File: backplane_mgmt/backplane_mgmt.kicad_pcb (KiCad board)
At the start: 2 copper layers, 160 x 100 mm, 86 parts, among them J101 AudioJack3, J201 Backplane, J304 VIn, Q301 SUD19P06-60, Q302 SUD19P06-60, U101 LM833, U203 AT24CS32-SSHM, U301 AZ1117CD-5.0, U302 PTH08T220, U303 INA260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

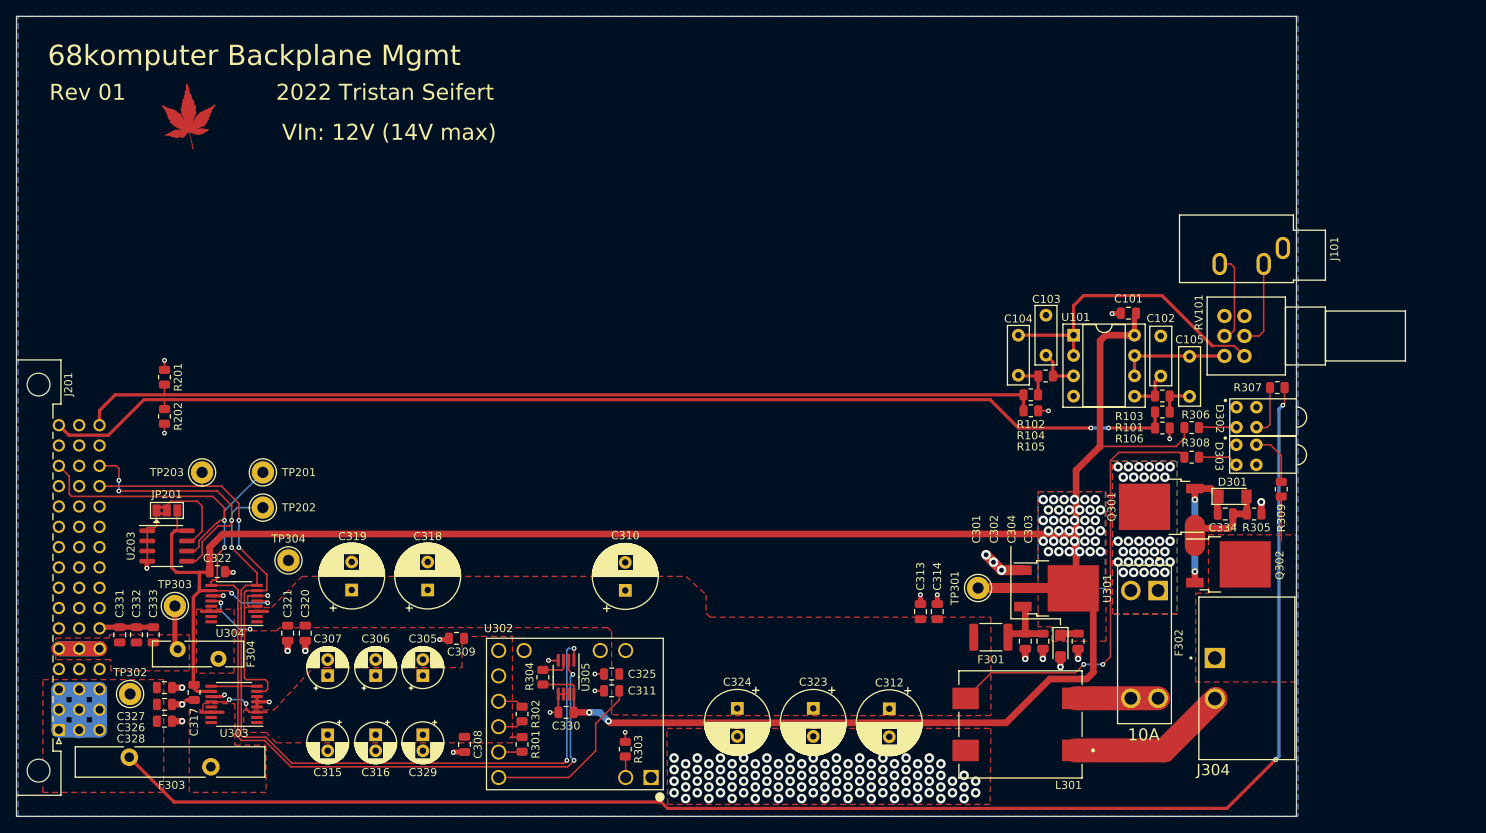
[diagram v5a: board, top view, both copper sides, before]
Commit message: Added +12V regulator to backplane mgmt
- Added the components for a discrete switching regulator (that is, with
  external switching MOSFETs, but a fancy little switching controller)
  to generate the 12V rail, at up to 10A. This is then further regulated
  to provide 5V for the board itself, and for the rest of the system.
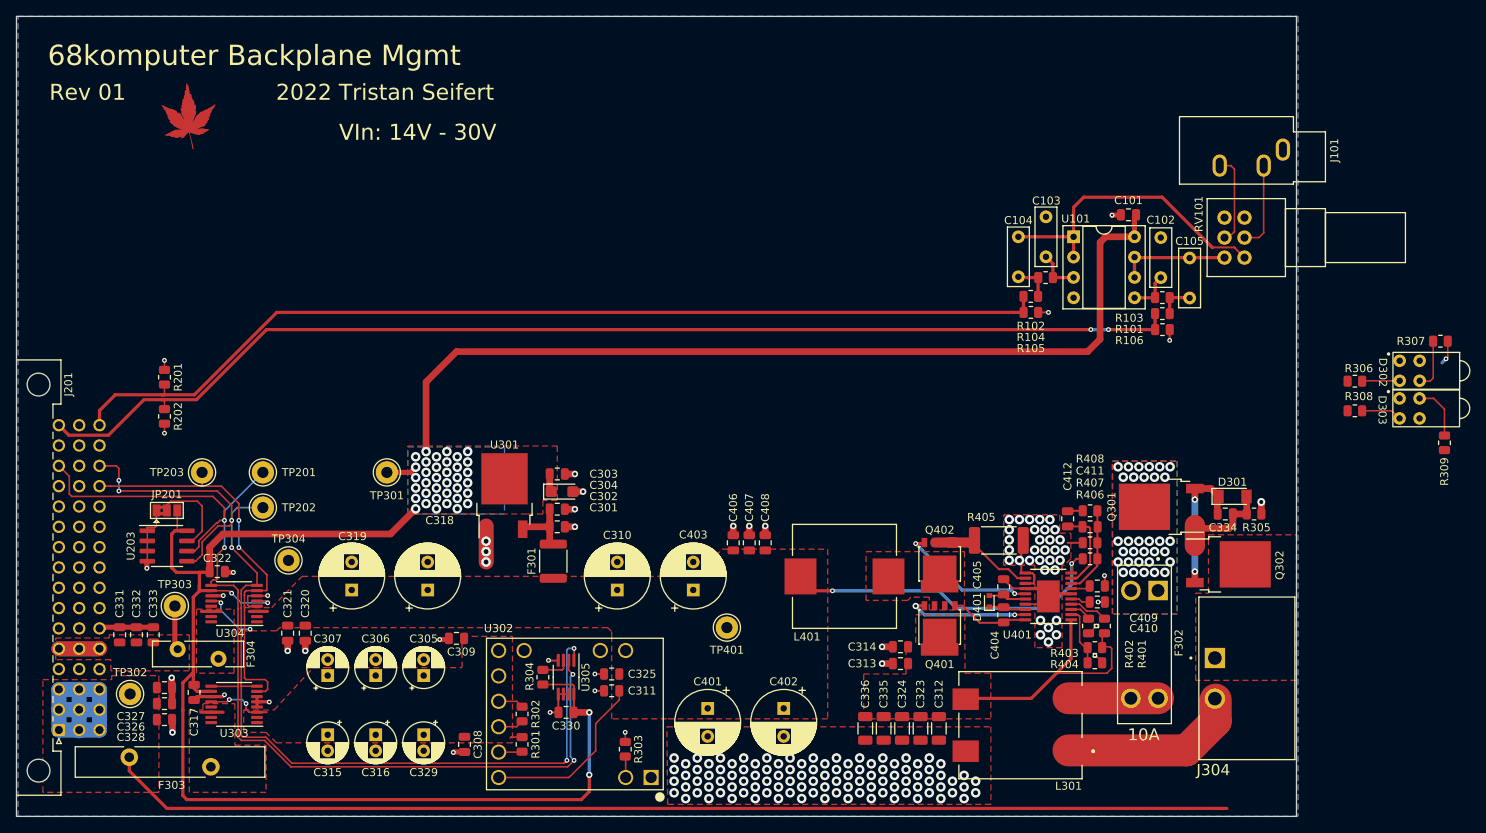
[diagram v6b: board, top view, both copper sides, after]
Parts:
- added C335: 2.2µF, Capacitor_SMD:C_1206_3216Metric, F.Cu at (138.4, 109.0)
- added C336: 2.2µF, Capacitor_SMD:C_1206_3216Metric, F.Cu at (136.1, 109.0)
- added C401: 330µF, Capacitor_THT:CP_Radial_D8.0mm_P3.50mm, F.Cu at (116.4, 106.5)
- added C402: 330µF, Capacitor_THT:CP_Radial_D8.0mm_P3.50mm, F.Cu at (125.9, 106.5)
- added C403: 330µF, Capacitor_THT:CP_Radial_D8.0mm_P3.50mm, F.Cu at (114.6, 91.7)
- added C404: 1µF, Capacitor_SMD:C_0805_2012Metric, F.Cu at (153.4, 94.8)
- added C405: 1µF, Capacitor_SMD:C_0805_2012Metric, F.Cu at (153.4, 91.3)
- added C406: 1µF, Capacitor_SMD:C_0805_2012Metric, F.Cu at (119.6, 85.8)
- added C407: 1µF, Capacitor_SMD:C_0805_2012Metric, F.Cu at (121.6, 85.8)
- added C408: 100nF, Capacitor_SMD:C_0805_2012Metric, F.Cu at (123.6, 85.8)
- added C409: 100nF, Capacitor_SMD:C_0805_2012Metric, F.Cu at (165.1, 91.2)
- added C410: 330pF, Capacitor_SMD:C_0805_2012Metric, F.Cu at (165.1, 93.2)
- added C411: 15pF, Capacitor_SMD:C_0805_2012Metric, F.Cu at (164.2, 83.8)
- added C412: 150pF, Capacitor_SMD:C_0805_2012Metric, F.Cu at (161.4, 82.8)
- added D401: BAS516, Diode_SMD:D_SOD-523, F.Cu at (151.6, 93.1)
- added L401: 2.7µH, 68komputer-common:Bourns_Inc.-SRP1250-0-0-MFG, F.Cu at (133.5, 90.0)
- added Q401: PSMN045-80YS, Package_TO_SOT_SMD:LFPAK56, F.Cu at (145.4, 96.5)
- added Q402: PSMN045-80YS, Package_TO_SOT_SMD:LFPAK56, F.Cu at (145.4, 88.6)
- added R401: 1M, Resistor_SMD:R_0805_2012Metric, F.Cu at (166.0, 96.2)
- added R402: 5k23, Resistor_SMD:R_0805_2012Metric, F.Cu at (164.0, 96.2)
- added R403: 23k7, Resistor_SMD:R_0805_2012Metric, F.Cu at (164.8, 98.9)
- added R404: 2k87, Resistor_SMD:R_0805_2012Metric, F.Cu at (164.8, 100.8)
- added R405: 3mΩ, Resistor_SMD:R_2512_6332Metric_Pad1.40x3.35mm_HandSolder, F.Cu at (152.8, 85.5)
- added R406: 86k6, Resistor_SMD:R_0805_2012Metric, F.Cu at (164.2, 87.8)
- added R407: 9k76, Resistor_SMD:R_0805_2012Metric, F.Cu at (164.2, 85.8)
- added R408: 133k, Resistor_SMD:R_0805_2012Metric, F.Cu at (164.2, 81.8)
- added TP401: VDD, TestPoint:TestPoint_Loop_D2.60mm_Drill1.4mm_Beaded, F.Cu at (118.8, 96.4)
- added U401: LM25116, Package_SO:HTSSOP-20-1EP_4.4x6.5mm_P0.65mm_EP2.85x4mm, F.Cu at (159.0, 92.5)
- C312, C323, C324: value 330µF -> 2.2µF; footprint Capacitor_THT:CP_Radial_D8.0mm_P3.50mm -> Capacitor_SMD:C_1206_3216Metric
- moved TP301 75.3 mm to (76.3, 77.0), turned to 0 degrees
- moved U301 70.0 mm to (91.0, 79.9), turned to 90 degrees
- moved C303 68.4 mm to (97.6, 77.2), turned to 0 degrees
- moved C304 65.2 mm to (98.2, 79.4), turned to 0 degrees
- moved C302 62.9 mm to (97.6, 81.6), turned to 180 degrees
- moved C301 60.2 mm to (97.6, 83.8), turned to 180 degrees
- moved F301 55.5 mm to (97.1, 88.1), turned to 90 degrees
- moved R306 21.2 mm to (197.3, 65.6)
- moved D302 21.2 mm to (210.4, 64.3)
- moved D303 21.2 mm to (210.4, 69.0)
- moved R307 21.2 mm to (208.0, 60.6)
- moved R308 21.2 mm to (197.3, 69.3)
- moved R309 21.2 mm to (208.5, 73.3)
- moved C324 20.8 mm to (140.7, 109.0)
- moved C323 13.6 mm to (143.0, 109.0)
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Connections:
- C310 pad 1: VBUS -> VDD
- C311 pad 1: VBUS -> VDD
- C318 pad 1: VBUS -> VDD
- C319 pad 1: VBUS -> VDD
- C320 pad 1: VBUS -> VDD
- C321 pad 1: VBUS -> VDD
- C325 pad 1: VBUS -> VDD
- F301 pad 1: VBUS -> VDD
- U302 pad 10: VBUS -> VDD
- U302 pad 2: VBUS -> VDD
- U304 pad 1: VBUS -> VDD
- U304 pad 12: VBUS -> VDD
- U304 pad 2: VBUS -> VDD
- U304 pad 3: VBUS -> VDD
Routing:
- net VDD: track 0.00 -> 73.0 mm, vias 0 -> 4
- net VBUS: track 86.0 -> 32.7 mm, vias 4 -> 0
- net +5V: track 225.9 -> 174.3 mm, vias 2 -> 1
- net +5VA: track 312.3 -> 284.6 mm
- net GND: track 68.3 -> 94.7 mm, vias 136 -> 174
- net Net-(Q402-Pad4): track 0.00 -> 17.4 mm, vias 0 -> 2
- net Net-(Q401-Pad4): track 0.00 -> 15.3 mm, vias 0 -> 2
- net Net-(Q402-Pad1): track 0.00 -> 13.6 mm
- net /Power/12V boi/FB: track 0.00 -> 11.0 mm
- net /Power/12V boi/COMP: track 0.00 -> 10.6 mm
- net /Power/12V boi/SW: track 0.00 -> 9.63 mm
- net Net-(R403-Pad1): track 0.00 -> 7.44 mm
- net /Power/VIn: track 5.59 -> 0.00 mm
- net Net-(R401-Pad1): track 0.00 -> 4.91 mm
- net /SNDL: track 121.4 -> 126.0 mm
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- added copper zone on F.Cu, net /Power/12V boi/SW
- added copper zone on F.Cu, net VDD
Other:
- board text added: "+VIn"
- board text added: "VIn: 14V - 30V"
- board text removed: "+12V"
- board text removed: "VIn: 12V (14V max)"

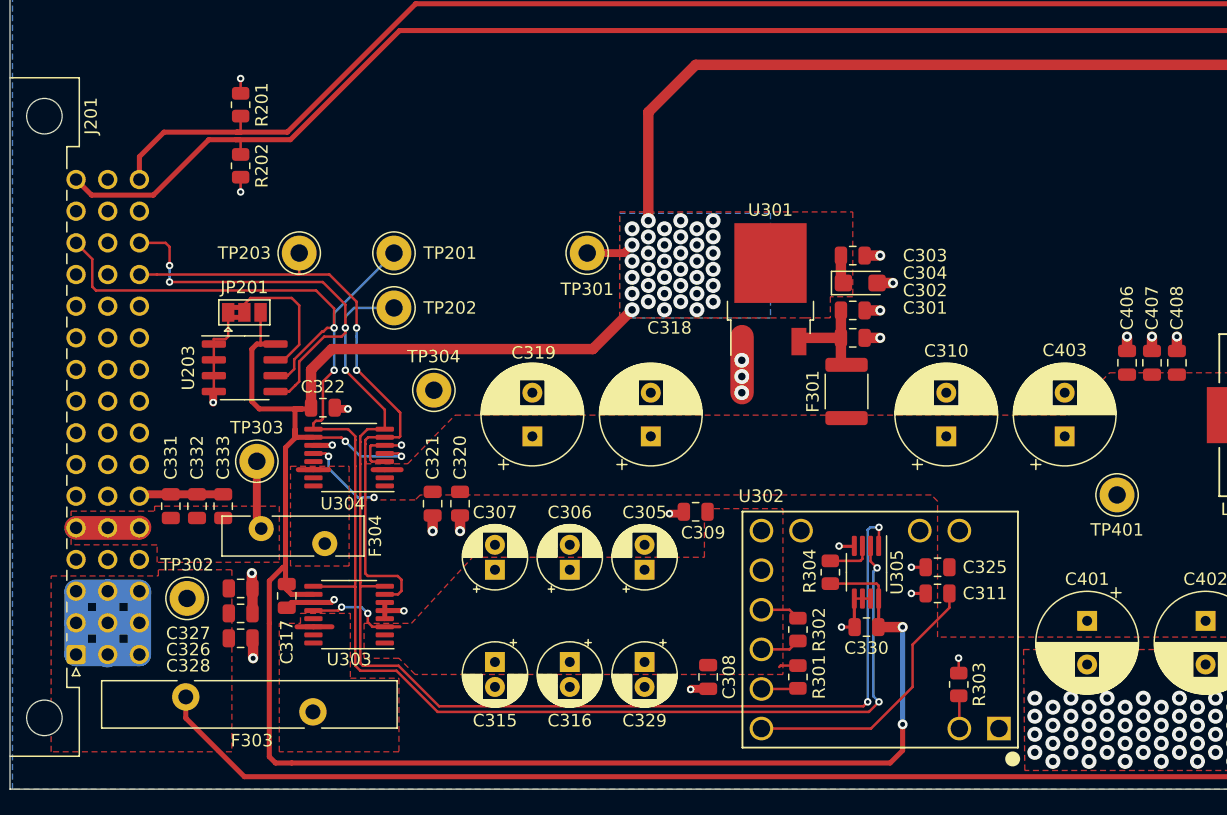
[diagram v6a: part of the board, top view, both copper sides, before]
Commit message: Replaced current sense with shunt+INA209
- Instead of using unobtanium parts for the current sensing, we're
  instead just gonna use more of the shunt we already have to get for
  the current limit of the switching regulator, and then measuring the
  voltage drop with the INA209 which is functionally going to give us
  the same exact behavior as before.
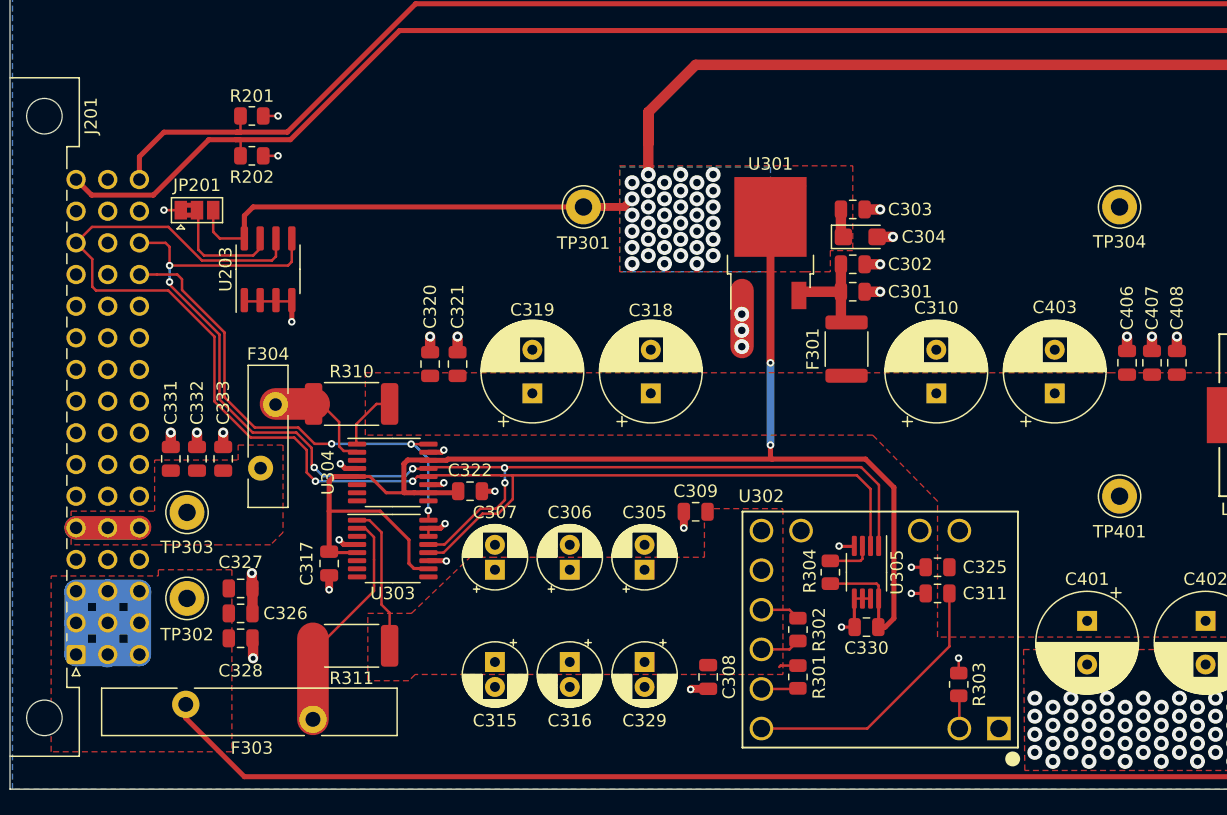
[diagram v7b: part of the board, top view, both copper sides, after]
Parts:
- removed TP201: SCL, TestPoint:TestPoint_Loop_D2.60mm_Drill1.4mm_Beaded
- removed TP202: SDA, TestPoint:TestPoint_Loop_D2.60mm_Drill1.4mm_Beaded
- removed TP203: ~{IRQ}, TestPoint:TestPoint_Loop_D2.60mm_Drill1.4mm_Beaded
- added R310: 3mΩ, Resistor_SMD:R_2512_6332Metric_Pad1.40x3.35mm_HandSolder, F.Cu at (57.4, 89.1)
- added R311: 3mΩ, Resistor_SMD:R_2512_6332Metric_Pad1.40x3.35mm_HandSolder, F.Cu at (57.4, 108.5)
- U303, U304: value INA260 -> INA209
- moved TP304 56.9 mm to (119.0, 73.3)
- moved C322 13.6 mm to (66.9, 96.1)
- moved C320 11.5 mm to (63.7, 85.9), turned to 90 degrees
- moved C321 11.4 mm to (65.9, 85.9), turned to 90 degrees
- moved JP201 9.04 mm to (45.0, 73.6)
- moved U203 8.12 mm to (50.7, 78.3), turned to 90 degrees
- moved TP303 6.94 mm to (44.2, 97.8)
- moved U303 6.35 mm to (60.7, 100.7), turned to 0 degrees
- moved F304 4.85 mm to (50.1, 94.2), turned to 90 degrees
- moved C317 4.28 mm to (55.6, 101.9)
- moved C331 3.80 mm to (42.9, 93.5)
- moved C332 3.80 mm to (45.0, 93.5)
- moved C333 3.80 mm to (47.1, 93.5)
- moved TP301 3.71 mm to (76.0, 73.3)
- moved C301 3.70 mm to (97.6, 80.1)
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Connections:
- U303 pad 12: /Power/+5V_PRE -> /SCL
- U303 pad 13: unconnected-(U303-Pad13) -> /SDA
- U303 pad 14: /Power/+5V_POST -> GND
- U303 pad 15: /Power/+5V_POST -> GND
- U303 pad 16: /Power/+5V_POST -> /~{IRQ}
- U303 pad 2: /Power/+5V_PRE -> /Power/+5V_POST
- U303 pad 3: /Power/+5V_PRE -> unconnected-(U303-Pad3)
- U303 pad 5: GND -> +5VA
- U303 pad 6: GND -> unconnected-(U303-Pad6)
- U303 pad 7: /~{IRQ} -> unconnected-(U303-Pad7)
- U303 pad 8: /SDA -> unconnected-(U303-Pad8)
- U303 pad 9: /SCL -> unconnected-(U303-Pad9)
- U304 pad 12: VDD -> /SCL
- U304 pad 13: unconnected-(U304-Pad13) -> /SDA
- U304 pad 14: /Power/12V_PRE -> +5VA
- U304 pad 15: /Power/12V_PRE -> GND
- U304 pad 16: /Power/12V_PRE -> /~{IRQ}
- U304 pad 2: VDD -> /Power/12V_PRE
- U304 pad 3: VDD -> unconnected-(U304-Pad3)
- U304 pad 6: GND -> unconnected-(U304-Pad6)
- U304 pad 7: /~{IRQ} -> unconnected-(U304-Pad7)
- U304 pad 8: /SDA -> unconnected-(U304-Pad8)
- U304 pad 9: /SCL -> unconnected-(U304-Pad9)
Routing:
- net /SDA: track 126.4 -> 100.5 mm
- net /SCL: track 131.8 -> 111.8 mm, vias 4 -> 2
- net +5VA: track 284.6 -> 269.0 mm, vias 40 -> 38
- net /Power/+5V_POST: track 2.80 -> 17.8 mm
- net /~{IRQ}: track 51.5 -> 39.2 mm, vias 2 -> 3
- net GND: track 94.7 -> 86.6 mm, vias 174 -> 181
- net /Power/12V_PRE: track 2.45 -> 8.69 mm
- net +12V: track 15.7 -> 10.2 mm
- net VDD: track 73.0 -> 69.1 mm, vias 4 -> 2
- net /Power/+5V_PRE: track 9.66 -> 13.3 mm, vias 2 -> 0
- net Net-(JP201-Pad2): track 10.8 -> 9.33 mm
- net Net-(C301-Pad2): track 6.96 -> 7.71 mm
- removed copper zone on F.Cu, net /Power/+5V_POST
- removed copper zone on F.Cu, net /Power/12V_PRE
